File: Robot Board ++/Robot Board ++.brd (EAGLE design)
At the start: 68.6 x 76.2 mm, 58 parts

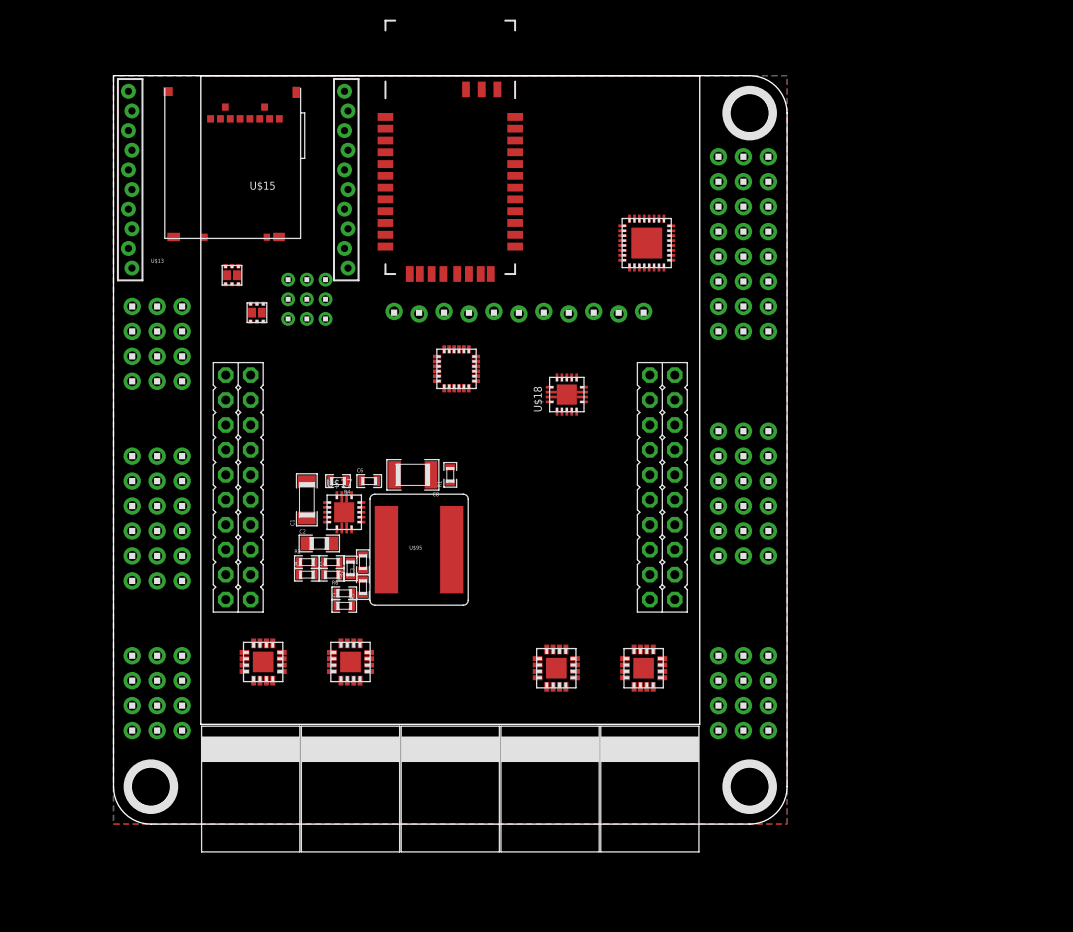
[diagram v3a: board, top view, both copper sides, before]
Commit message: Nearly completed Schematic layout Components on board are being arranged Upgraded to TPS53319 (14A w/ smaller Inductor) Need to find more IO for GPIO pins (consider using PCA9534 IO Expander) Most passives added Added INA220 Power monitor Considering using a buffer for signals (Card Detect, XBee, Bluetooth, Power Good, etc...)
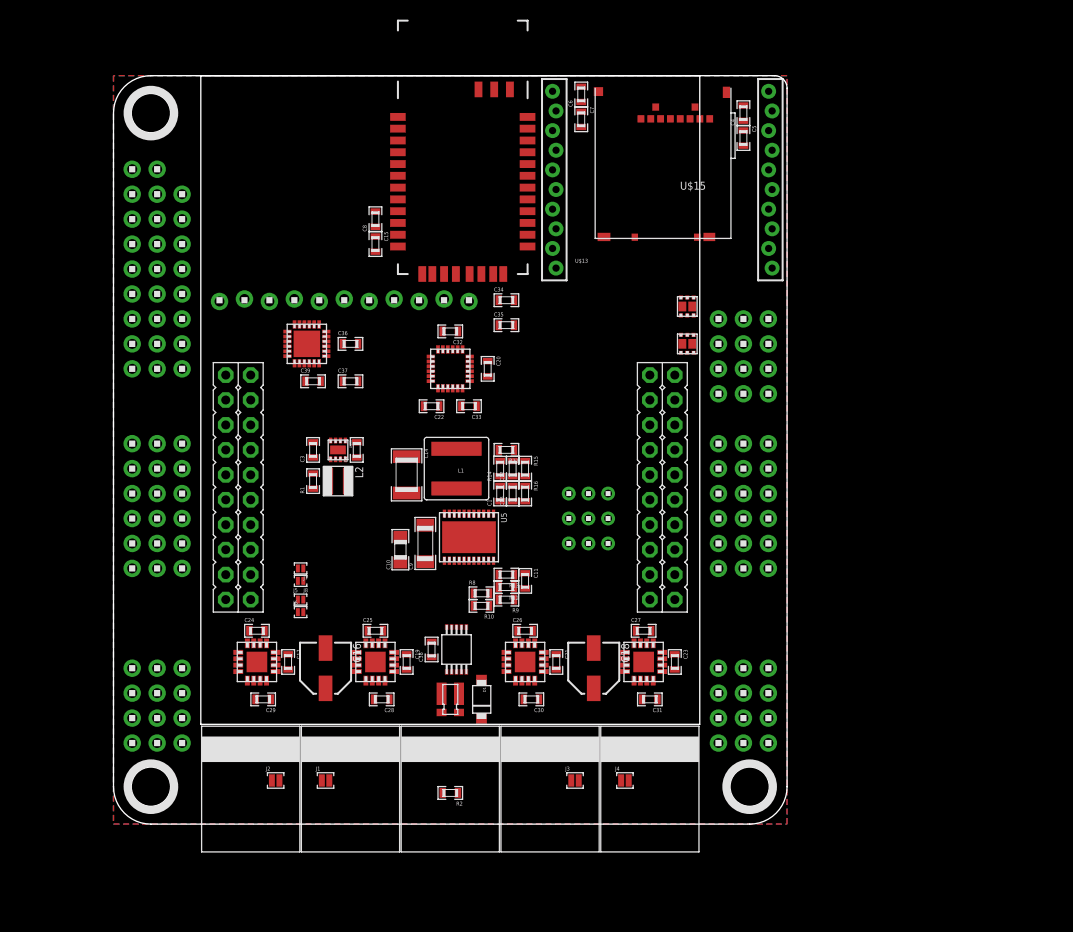
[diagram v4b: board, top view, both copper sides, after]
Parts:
- removed R4: 182k, standardparts:0603
- removed R5: 1.81k, standardparts:0603
- removed R6: 16.5k, standardparts:0603
- removed R7: 2.21k, standardparts:0603
- removed U$16: ADS7953.RHB, packages(ti):RHB.32
- removed U$17, U$18: TPS54X21.RHL, packages(ti):RHL.14
- added C10: 4.7uF, standardparts:0805
- added C11, C15, C35, C37: 1uF, standardparts:0603
- added C12, C17, C19, C20, C21, C23, C24, C25, C26, C27, C28, C29, C30, C31, C33, C34, C36, C38, C39: .1uF, standardparts:0603
- added C13: 1nF, standardparts:0603
- added C14: 100uF, standardparts:1210
- added C16, C18: 100uF, microbuilder:PANASONIC_C
- added C22, C32: 10nF, standardparts:0603
- added C9: 22uF, standardparts:1206
- added D1: (no value), nxp:SOD123W
- added J1, J2, J3, J4: (no value), solderjumper:2.LRG
- added J5, J6, J7, J8: (no value), solderjumper:2.MED
- added L1: 2.2uH, coilcraft:XAL6030
- added L2: 1uH, bourns:SRN3015
- added R10: 1k, standardparts:0603
- added R11, R12: 100k, standardparts:0603
- added R13: 191k, standardparts:0603
- added R14: 2.55k, standardparts:0603
- added R15: 76.8k, standardparts:0603
- added R16: 10k, standardparts:0603
- added R8: 200k, standardparts:0603
- added R9: 86.6k, standardparts:0603
- added U$107: 1X2, headers(.1in):1X2
- added U$118: INA220.DGS, packages(ti):DGS.10
- added U$98: ADS7959.RGE, packages(ti):RGE.24
- added U5: TPS5331[8/9].DQP, packages(ti):DQP.22
- C1: value 22uF -> .1uF; device standardparts:1206 -> standardparts:0603
- C2: value 4.7uF -> 10uF; device standardparts:0805 -> standardparts:0603
- C3: value 22nF -> 22uF
- C4: value 47nF -> .1uF
- C5: value 390pF -> 1uF
- C7: value 1nF -> 1uF
- C8: value 100uF -> .1uF; device standardparts:1210 -> standardparts:0603
- R1: value 49.9k -> 178k
- R2: value 31.2k -> 100k
- R3: value 8.45 -> 1u; device standardparts:0603 -> vishay:0612
- U$1, U$2, U$5: value 1X6 -> 1X8; device headers(.1in):1X6 -> headers(.1in):1X8
- U$6, U$7, U$9: value 1X8 -> 1X6; device headers(.1in):1X8 -> headers(.1in):1X6
- U$95: value XAL1010-682 -> TPS62082.DSG; device coilcraft:XAL1010 -> packages(ti):DSG
- moved U$6 77.1 mm to (1.91, 26.0), turned to 90 degrees
- moved U$7 72.9 mm to (4.45, 26.0), turned to 90 degrees
- moved U$9 68.8 mm to (6.99, 26.0), turned to 90 degrees
- moved U$1 67.5 mm to (1.91, 46.4)
- moved U$35 64.8 mm to (66.7, 43.8)
- moved U$38 64.8 mm to (66.7, 26.0)
- moved C4 63.0 mm to (64.1, 72.4), turned to 90 degrees
- moved U$2 62.7 mm to (4.45, 46.4)
- moved U$11 61.0 mm to (3.81, 72.4)
- moved C5 60.2 mm to (64.1, 69.8), turned to 270 degrees
- moved U$36 59.7 mm to (64.1, 43.8)
- moved U$39 59.7 mm to (64.1, 26.0)
- moved U$5 57.8 mm to (6.99, 46.4)
- moved C7 55.1 mm to (47.6, 71.8), turned to 270 degrees
- moved U$37 54.6 mm to (61.6, 43.8)
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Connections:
- removed net AD6: U$16.14, U$9.7
- removed net AD7: U$16.13, U$9.8
- removed net LS.PWR: U$61.10
- removed net M.!SLP: U1.3, U2.3, U3.3, U4.3
- removed net VDD: U$13.1
- new net 3.3V.PG: R1.1, U$95.6
- new net 5V.PG: R11.2, U$95.1, U5.3
- new net M.EN: R2.1, U1.3, U2.3, U3.3, U4.3
- new net M.MODE: U1.16, U2.16, U3.16, U4.16
- new net M0.DIR: J6.1, U1.4
- new net M0.SPD: J5.1, U$8.PD0, U1.1
- new net M1.DIR: J6.2, U2.4
- new net M1.SPD: J5.2, U$8.PD1, U2.1
- new net M2.DIR: J8.1, U3.4
- new net M2.SPD: J7.1, U$8.PA6, U3.1
- new net M3.DIR: J8.2, U4.4
- new net M3.SPD: J7.2, U$8.PA7, U4.1
- new net N$11: R10.1, R8.2, R9.2
- new net N$14: C12.1, C13.2, R14.2
- new net N$15: C1.2, L1.1, R14.1, U5.10, U5.11, U5.6, U5.7, U5.8, U5.9
- new net N$16: U$8.PA4
- new net N$17: U$8.PA5
- new net N$18: C24.2, U1.13
- new net N$19: C25.2, U2.13
- new net N$20: C26.2, U3.13
- new net N$21: C27.2, U4.13
- new net N$22: D1.P$2, R3.1@1, R3.1@2, U$118.10, U$60.1
- new net N$24: C32.1, U$59.20
- new net N$25: C19.1, U2.11
- new net N$27: C21.1, U3.11
- new net N$29: C23.1, U4.11
- new net N$30: U$8.PF4
- new net N$31: U$8.PF3
- new net N$32: U$8.PF2
- new net N$33: U$8.PF1
- new net N$34: U$8.PF0
- new net N$37: C21.2, U3.10
- new net N$38: C17.2, U1.10
- new net N$39: C19.2, U2.10
- new net N$40: C23.2, U4.10
- new net N$44: U$8.PB3
- new net N$45: U$8.PB2
- new net N$46: U$8.PB0
- new net N$47: U$8.PB1
- new net SCL: U$118.5
- new net SDA: U$118.4
- new net SVRO6: U$5.7, U$8.PC4
- new net SVRO7: U$5.8, U$8.PC5
- new net XBEE.RSSI: U$13.6
- net 3.3V: now also C15.1, C20.1, C22.1, C3.1, C38.1, C39.1, C4.1, C5.1, C6.1, C7.1, C8.1, L2.2, R1.2, U$118.6, U$13.1, U$14.11, U$15.VDD, U$59.13, U$59.8, U$7.1, U$7.2, U$7.3, U$7.4, U$7.5, U$7.6, U$95.5, U$98.21
- net 5.0V: now also C12.2, C14.1, C2.1, L1.2, R15.1, U$107.1, U$2.7, U$2.8, U$95.8; no longer C7.1, C8.1, R6.1, U$17.7, U$95.P$2
- net AD0: now also U$8.PE3; no longer U$16.20
- net AD1: now also U$8.PE2; no longer U$16.19
- net AD2: now also U$8.PE1; no longer U$16.18
- net AD3: now also U$8.PE0; no longer U$16.17
- net AD4: now also U$8.PD3; no longer U$16.16
- net AD5: now also U$8.PD2; no longer U$16.15
- net ADS.!CS: now also U$98.16; no longer U$16.23
- net ADS.ALARM: now also U$98.22; no longer U$16.29
- net ADS.MISO: now also U$98.18; no longer U$16.25
- net ADS.MOSI: now also U$98.19; no longer U$16.26
- net ADS.SCLK: now also U$98.17; no longer U$16.24
- net BT.RXI: now also U$8.PD6
- net BT.TXO: now also U$8.PD7
- net GND: now also C10.2, C11.1, C14.2, C15.2, C16.-, C18.-, C20.2, C22.2, C24.1, C25.1, C26.1, C27.1, C28.2, C29.2, C3.2, C30.2, C31.2, C32.2, C33.1, C34.2, C35.2, C36.2, C37.2, C38.2, C39.2, C4.2, C6.2, C7.2, C9.2, D1.P$1, R12.1, R13.2, R16.2, R2.2, R9.1, U$1.7, U$1.8, U$107.2, U$118.1, U$118.2, U$118.7, U$59.1, U$59.11, U$60.2, U$95.2, U$95.3, U$95.PAD, U$98.15, U$98.2, U$98.20, U$98.23, U$98.5, U$98.PAD, U5.PAD; no longer C1.2, C3.1, C4.1, R3.2, R4.1, R7.2, U$16.1, U$16.22, U$16.27, U$16.30, U$16.4, U$16.PAD, U$17.2, U$17.3, U$17.PAD, U$18.2, U$18.3, U$18.PAD, U$6.7, U$6.8
- net LS.1: now also U$98.6; no longer U$16.5
- net LS.2: now also U$98.7; no longer U$16.6
- net LS.3: now also U$98.8; no longer U$16.7
- net LS.4: now also U$98.9; no longer U$16.8
- net LS.5: now also U$98.10; no longer U$16.9
- net LS.6: now also U$98.11; no longer U$16.10
- net LS.7: now also U$98.12; no longer U$16.11
- net LS.8: now also U$98.13; no longer U$16.12
- net M0+: now also J1.1
- net M0-: now also J2.1
- net M1+: now also J1.2
- net M1-: now also J2.2
- net M2+: now also J3.1
- net M2-: now also J4.1
- net M3+: now also J3.2
- net M3-: now also J4.2
- net N$1: now also U$8.PA2; no longer R2.2, R3.1, U$17.10
- net N$10: now also C13.1, R15.2, R16.1, U5.1; no longer C6.2, U$17.11, U$17.12, U$95.P$1
- net N$12: now also L2.1, U$95.7; no longer C7.2, R6.2, R7.1
- net N$13: now also C17.1, U1.11; no longer U$16.31
- net N$2: now also C1.1, U5.4; no longer R1.2, U$17.14
- net N$3: now also R12.2, U5.20; no longer C4.2, R5.1
- net N$4: now also C11.2, R11.1, U5.18; no longer C5.1, R5.2, U$17.8
- net N$5: now also R13.1, U5.21; no longer C3.2, U$17.9
- net N$6: now also U$98.3, U$98.4; no longer U$16.2, U$16.3
- net N$7: now also C33.2, U$59.10; no longer U$16.21, U$16.28, U$16.32
- net N$8: now also R10.2, U5.2; no longer R4.2, U$17.1
- net N$9: now also U$8.PA3; no longer C6.1, U$17.13
- net SVRO0: now also U$8.PB6
- net SVRO1: now also U$8.PB7
- net SVRO2: now also U$8.PB4
- net SVRO3: now also U$8.PB5
- net SVRO4: now also U$8.PE4
- net SVRO5: now also U$8.PE5
- net VBAT: now also C10.1, C16.+, C18.+, C28.1, C29.1, C30.1, C31.1, C9.1, R3.2@1, R3.2@2, R8.1, U$118.8, U$118.9, U1.8, U2.8, U3.8, U4.8, U5.12, U5.13, U5.14, U5.15, U5.16, U5.17, U5.19; no longer C1.1, C2.1, R1.1, R2.1, U$17.4, U$17.5, U$17.6
- net VCC: now also C34.1, C35.1, C36.1, C37.1, U$61.10, U$98.1, U$98.14, U$98.24; no longer U$7.1, U$7.2, U$7.3, U$7.4, U$7.5, U$7.6, U$7.7, U$7.8
- net VIN: now also U$55.6, U$55.PAD@1, U$56.6, U$56.PAD@1
- net XBEE.RXI: now also U$8.PC6
- net XBEE.TXO: now also U$8.PC7
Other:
- outline, holes or cut-outs redrawn
- board text added: "ADC"
- board text added: "ENC[0/1]"
- board text added: "ENC[2/3]"
- board text added: "GPIO"
- board text added: "MOSFET"
- board text added: "SERVO"

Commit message: Schematic tenatively completed. Changed Encoders to SPI (AS5050) Went down from 4 to 2 MOSFETs Went down from 16 to 6 IO Using 8 ADC to I2C converter for line sensor Pinouts finalized. Added indicator LEDs for debugging purposes.
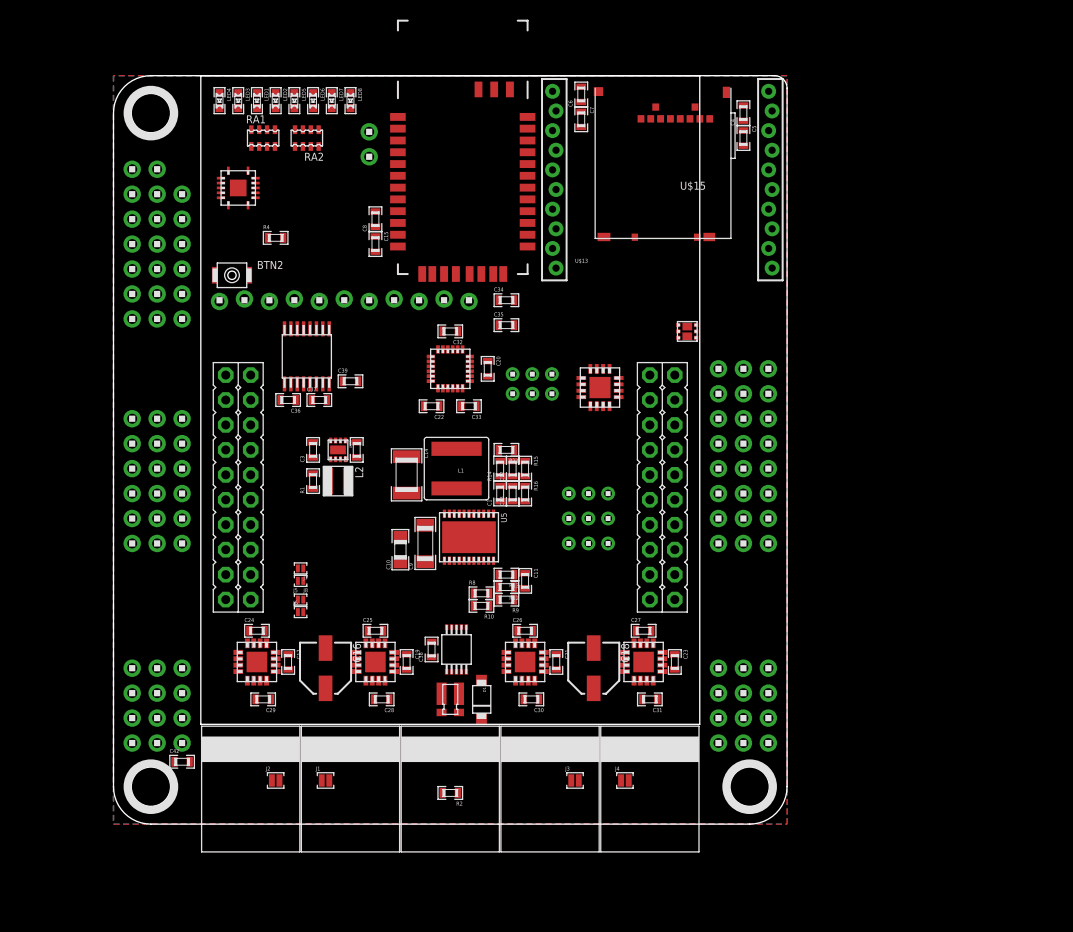
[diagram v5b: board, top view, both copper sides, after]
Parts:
- removed U$56: FDMA1024NZ, freescale:MICROFET.2X2
- removed U$98: ADS7959.RGE, packages(ti):RGE.24
- added BTN2: B3U-1000P(M)-B, omron:B3U-1000P(M)-B
- added C42: .1uF, standardparts:0603
- added LED1, LED2, LED3, LED4, LED5, LED6, LED7, LED8: (no value), standardparts:0603.LED
- added R4: 1k, standardparts:0603
- added RA1, RA2: 1k, resistorarray:0603.4.C
- added U$123: PCA9557.RGV, packages(ti):RGV.16
- added U$126: ADS7830.PW, packages(ti):PW.16
- added U$131: 2X3, headers(2mm):2X3
- added U$132: 74XX125.RGY, packages(ti):RGY.14
- added U$135: 1X2, headers(.1in):1X2
- U$1, U$2, U$5: value 1X8 -> 1X6; device headers(.1in):1X8 -> headers(.1in):1X6
- U$35, U$36, U$37: value 1X4 -> 1X2; device headers(.1in):1X4 -> headers(.1in):1X2
- moved C36 8.54 mm to (17.8, 43.2), turned to 180 degrees
- moved U$1 5.08 mm to (1.91, 51.4)
- moved U$2 5.08 mm to (4.45, 51.4)
- moved U$5 5.08 mm to (6.99, 51.4)
- moved C39 3.81 mm to (24.1, 45.1)
- moved C37 3.70 mm to (21.0, 43.2)
- moved U$107 2.54 mm to (4.45, 66.7), turned to 180 degrees
- moved U$38 2.54 mm to (66.7, 28.6)
- moved U$39 2.54 mm to (64.1, 28.6)
- moved U$40 2.54 mm to (61.6, 28.6)
- moved U$6 2.54 mm to (1.91, 28.6)
- moved U$7 2.54 mm to (4.45, 28.6)
- moved U$9 2.54 mm to (6.99, 28.6)
- moved U$55 1.27 mm to (58.4, 50.2), turned to 270 degrees
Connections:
- removed net ADS.!CS: U$98.16
- removed net ADS.ALARM: U$98.22
- removed net ADS.MISO: U$98.18
- removed net ADS.MOSI: U$98.19
- removed net ADS.SCLK: U$98.17
- removed net E0.A: U$43.3
- removed net E0.B: U$43.4
- removed net E1.A: U$44.3
- removed net E1.B: U$44.4
- removed net E2.A: U$45.3
- removed net E2.B: U$45.4
- removed net E3.A: U$46.3
- removed net E3.B: U$46.4
- removed net FET2: U$37.3, U$56.2
- removed net FET3: U$37.4, U$56.5
- removed net GND2: U$8.GND2
- removed net IMU.SCL: U$59.23
- removed net IMU.SDA: U$59.24
- removed net N$1: U$8.PA2
- removed net N$16: U$8.PA4
- removed net N$17: U$8.PA5
- removed net N$30: U$8.PF4
- removed net N$31: U$8.PF3
- removed net N$32: U$8.PF2
- removed net N$33: U$8.PF1
- removed net N$34: U$8.PF0
- removed net N$9: U$8.PA3
- removed net RST: U$8.RST
- removed net SD.!CS: U$15.!CS!/NC/DAT3
- removed net SD.DETECT: U$15.CD
- removed net SD.MISO: U$15.MISO/DAT0
- removed net SD.MOSI: U$15.MOSI/CMD
- removed net SD.SCLK: U$15.CLK
- removed net SVRO6: U$5.7, U$8.PC4
- removed net SVRO7: U$5.8, U$8.PC5
- new net BT.CONNECT: LED8.P$1, U$14.21
- new net BT.STATUS: LED7.P$1, U$14.19
- new net ENC0.!CS: U$43.5, U$8.PD6
- new net ENC1.!CS: U$45.5, U$8.PD7
- new net I2C.SCL: U$123.15, U$59.23, U$8.PB2
- new net I2C.SDA: U$123.16, U$59.24, U$8.PB3
- new net N$43: LED2.P$1, U$132.6
- new net N$48: LED5.P$2, RA2.7
- new net N$49: LED4.P$2, RA1.2
- new net N$50: LED3.P$1, U$132.8
- new net N$51: LED1.P$2, RA1.8
- new net N$52: LED2.P$2, RA1.6
- new net N$53: LED3.P$2, RA1.4
- new net SPI.FSS: U$15.!CS!/NC/DAT3, U$8.PA3
- new net SPI.MISO: U$15.MISO/DAT0, U$43.4, U$44.4, U$45.4, U$46.4, U$8.PA2
- new net SPI.MOSI: U$15.MOSI/CMD, U$43.6, U$44.6, U$45.6, U$46.6, U$8.PA5
- new net SPI.SCLK: U$15.CLK, U$43.3, U$44.3, U$45.3, U$46.3, U$8.PA4
- new net SVRO4/ENC2.!CS: U$44.5, U$8.PE4
- new net SVRO5/ENC3.!CS: U$46.5, U$8.PE5
- new net UART.RXI: U$131.3, U$132.5, U$8.PB0
- new net UART.TXO: U$131.4, U$132.2, U$8.PB1
- new net XBEE.ASSOCIATE: LED6.P$1, U$13.15
- net !RST: now also U$123.13, U$135.1, U$8.RST
- net 3.3V: now also BTN2.2, C42.1, U$123.14, U$126.16, U$132.14; no longer U$98.21
- net 3.3V.PG: now also U$132.12
- net 5.0V: no longer U$2.7, U$2.8
- net 5V.PG: now also U$132.9
- net BT.RESET: now also BTN2.1, R4.1
- net BT.RXI: now also U$131.5; no longer U$8.PD6
- net BT.TXO: now also U$131.6; no longer U$8.PD7
- net FET0: now also U$123.11
- net FET1: now also U$123.12
- net GND: now also C42.2, R4.2, RA1.1, RA1.3, RA1.5, RA1.7, RA2.1, RA2.4, RA2.6, RA2.8, U$123.1, U$123.2, U$123.3, U$123.6, U$123.PAD, U$126.11, U$126.12, U$126.13, U$126.9, U$132.1, U$132.10, U$132.13, U$132.4, U$132.7, U$132.PAD, U$135.2, U$8.GND1, U$8.GND2; no longer U$1.7, U$1.8, U$35.3, U$35.4, U$56.1, U$56.4, U$98.15, U$98.2, U$98.20, U$98.23, U$98.5, U$98.PAD
- net IO0: now also U$123.4
- net IO1: now also U$123.5
- net IO2: now also U$123.7
- net IO3: now also U$123.8
- net IO4: now also U$123.9
- net IO5: now also U$123.10
- net LS.1: now also U$126.1; no longer U$98.6
- net LS.2: now also U$126.2; no longer U$98.7
- net LS.3: now also U$126.3; no longer U$98.8
- net LS.4: now also U$126.4; no longer U$98.9
- net LS.5: now also U$126.5; no longer U$98.10
- net LS.6: now also U$126.6; no longer U$98.11
- net LS.7: now also U$126.7; no longer U$98.12
- net LS.8: now also U$126.8; no longer U$98.13
- net M0.DIR: now also U$8.PC4
- net M1.DIR: now also U$8.PC5
- net M2.DIR: now also U$8.PC6
- net M3.DIR: now also U$8.PC7
- net N$44: now also LED4.P$1, U$132.11; no longer U$8.PB3
- net N$45: now also LED8.P$2, RA2.2; no longer U$8.PB2
- net N$46: now also LED7.P$2, RA2.3; no longer U$8.PB0
- net N$47: now also LED6.P$2, RA2.5; no longer U$8.PB1
- net N$6: now also LED1.P$1, U$132.3; no longer U$98.3, U$98.4
- net SCL: now also U$126.14
- net SDA: now also U$126.15
- net SVRO4: no longer U$8.PE4
- net SVRO5: no longer U$8.PE5
- net VCC: now also U$126.10; no longer U$98.1, U$98.14, U$98.24
- net VIN: no longer U$36.3, U$36.4, U$56.6, U$56.PAD@1
- net XBEE.RSSI: now also LED5.P$1
- net XBEE.RXI: now also U$131.1; no longer U$8.PC6
- net XBEE.TXO: now also U$131.2; no longer U$8.PC7
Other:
- board text removed: "MOSFET"

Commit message: Completed Schematic (tenatively...)
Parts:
- removed U$1, U$2, U$5: 1X6, headers(.1in):1X6
- removed U$107, U$135, U$35, U$37: 1X2, headers(.1in):1X2
- removed U$131: 2X3, headers(2mm):2X3
- removed U$73, U$75, U$76: 1X3, headers(2mm):1X3
- added C40: .1uF, standardparts:0603
- added C41: 1uF, standardparts:0603
- added H10, H11, H12: 1X4, headers(.1in):1X4
- added H23: 2X3, headers(2mm):2X3
- added H24, H7, H8, H9: 1X2, headers(.1in):1X2
- added H25, H26, H27: 1X3, headers(2mm):1X3
- added R5: 100k, standardparts:0603
- added R6, R7: 2.2k, standardparts:0603
- J1, J2, J3, J4: device solderjumper:2.LRG -> solderjumper:2.XL
- moved U$55 49.6 mm to (10.8, 64.1), turned to 0 degrees
- moved U$123 40.0 mm to (12.1, 58.4), turned to 270 degrees
- moved BTN2 17.3 mm to (26.0, 66.0), turned to 270 degrees
- moved R4 14.8 mm to (26.7, 70.5), turned to 90 degrees
- moved C34 12.3 mm to (27.9, 50.8), turned to 180 degrees
- moved C35 9.53 mm to (30.5, 50.8)
- moved J1 7.62 mm to (14.0, 4.45), flipped to the bottom, turned to 180 degrees
- moved J2 7.62 mm to (24.1, 4.45), flipped to the bottom, turned to 180 degrees
- moved C37 7.24 mm to (16.5, 48.9), turned to 90 degrees
- moved U$132 5.24 mm to (17.8, 66.0)
- moved C36 3.42 mm to (16.5, 46.4), turned to 270 degrees
- moved C39 2.84 mm to (22.9, 47.6), turned to 90 degrees
- moved J3 2.54 mm to (44.5, 4.45), flipped to the bottom, turned to 180 degrees
- moved J4 2.54 mm to (54.6, 4.45), flipped to the bottom, turned to 180 degrees
- moved C4 1.91 mm to (64.1, 74.3)
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- renumbered U$29 to H17, U$30 to H18, U$32 to H19, U$33 to H20, U$36 to H22, U$38 to H1, U$39 to H2, U$40 to H3, U$43 to H13, U$44 to H15, U$45 to H14, U$46 to H16, U$6 to H4, U$60 to H21, U$7 to H5, U$9 to H6
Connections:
- removed net IMU.INT: U$59.12
- removed net IO4: H3.5, U$123.9
- removed net IO5: H3.6, U$123.10
- removed net LS.LED: U$61.9
- removed net SCL: U$118.5, U$126.14
- removed net SDA: U$118.4, U$126.15
- removed net VBUS: U$8.VBUS
- new net I2C.SDL: U$126.14
- net !RST: now also H24.1; no longer U$135.1
- net 3.3V: now also C40.1, C41.1, H25.1, H26.1, R6.1, R7.1; no longer U$73.1, U$75.1
- net 5.0V: now also H2.1, H2.2, H2.3, H2.4, H2.5, H2.6, H22.1, H25.3, H26.3, H27.1, U$8.VBUS; no longer U$107.1, U$2.1, U$2.2, U$2.3, U$2.4, U$2.5, U$2.6, U$73.3, U$75.3, U$76.1
- net BT.RXI: now also H23.5; no longer U$131.5
- net BT.TXO: now also H23.6; no longer U$131.6
- net FET0: now also H9.1, U$123.9; no longer U$123.11, U$37.1
- net FET1: now also H9.2, U$123.10; no longer U$123.12, U$37.2
- net GND: now also C40.2, C41.2, H10.1, H10.2, H10.3, H10.4, H22.2, H24.2, H7.1, H7.2; no longer U$1.1, U$1.2, U$1.3, U$1.4, U$1.5, U$1.6, U$107.2, U$135.2, U$35.1, U$35.2
- net I2C.SCL: now also R6.2, U$118.5
- net I2C.SDA: now also R7.2, U$118.4, U$126.15
- net IO0: now also H12.1; no longer H3.1
- net IO1: now also H12.2; no longer H3.2
- net IO2: now also H12.3; no longer H3.3
- net IO3: now also H12.4; no longer H3.4
- net M.EN: now also U$123.12
- net M.MODE: now also R5.2, U$123.11
- net SVRO0: now also H3.1; no longer U$5.1
- net SVRO1: now also H3.2; no longer U$5.2
- net SVRO2: now also H3.3; no longer U$5.3
- net SVRO3: now also H3.4; no longer U$5.4
- net SVRO4: now also H3.5; no longer U$5.5
- net SVRO5: now also H3.6; no longer U$5.6
- net UART.RXI: now also H23.3; no longer U$131.3
- net UART.TXO: now also H23.4; no longer U$131.4
- net VBAT: now also H27.3; no longer U$76.3
- net VCC: now also H26.2, U$61.9; no longer U$75.2
- net VDDIO: now also H11.1, H11.2, H11.3, H11.4, H25.2, R5.1; no longer H2.1, H2.2, H2.3, H2.4, H2.5, H2.6, U$73.2
- net VIN: now also H27.2, H8.1, H8.2; no longer H22.1, H22.2, U$76.2
- net XBEE.RXI: now also H23.1; no longer U$131.1
- net XBEE.TXO: now also H23.2; no longer U$131.2
